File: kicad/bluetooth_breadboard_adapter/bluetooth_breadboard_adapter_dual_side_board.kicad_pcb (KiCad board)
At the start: 2 copper layers, 24.9 x 36.1 mm, 4 parts, among them J1 SCJ368R1NUS0B00G, P1 CONNECTOR, P2 CONNECTOR, U1 BLK-MD-SPK-B

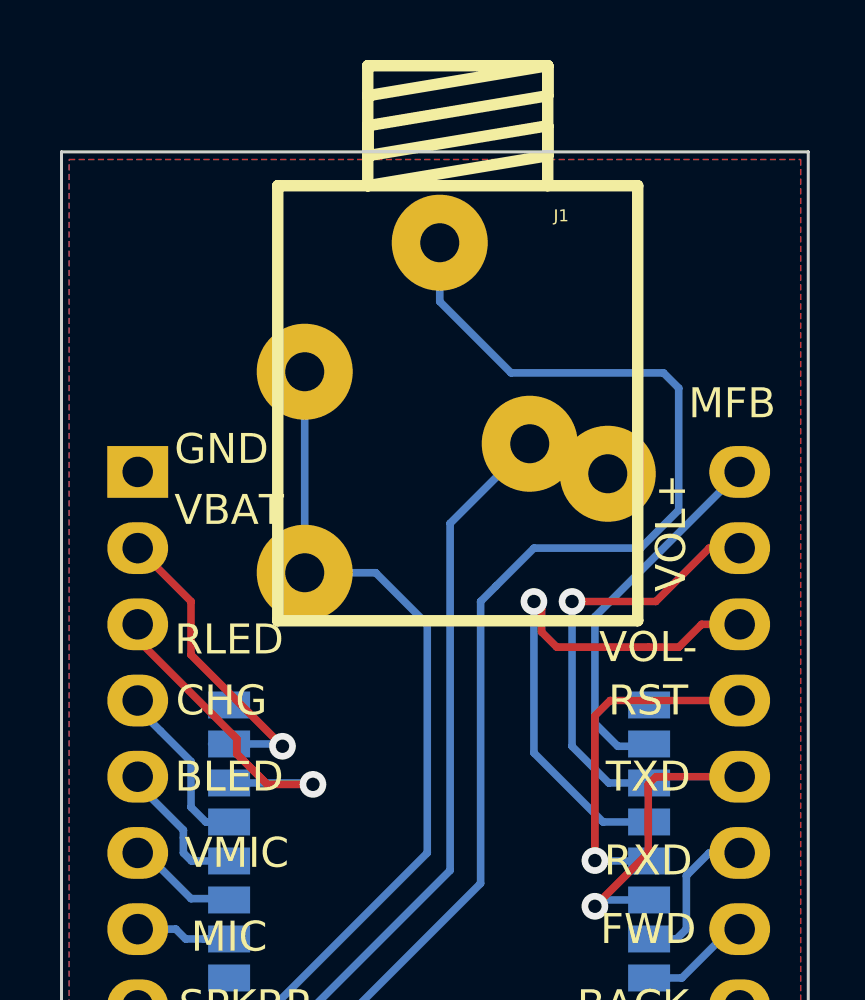
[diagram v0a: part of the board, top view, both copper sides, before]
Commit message: update patch to modules becouse of changed library name
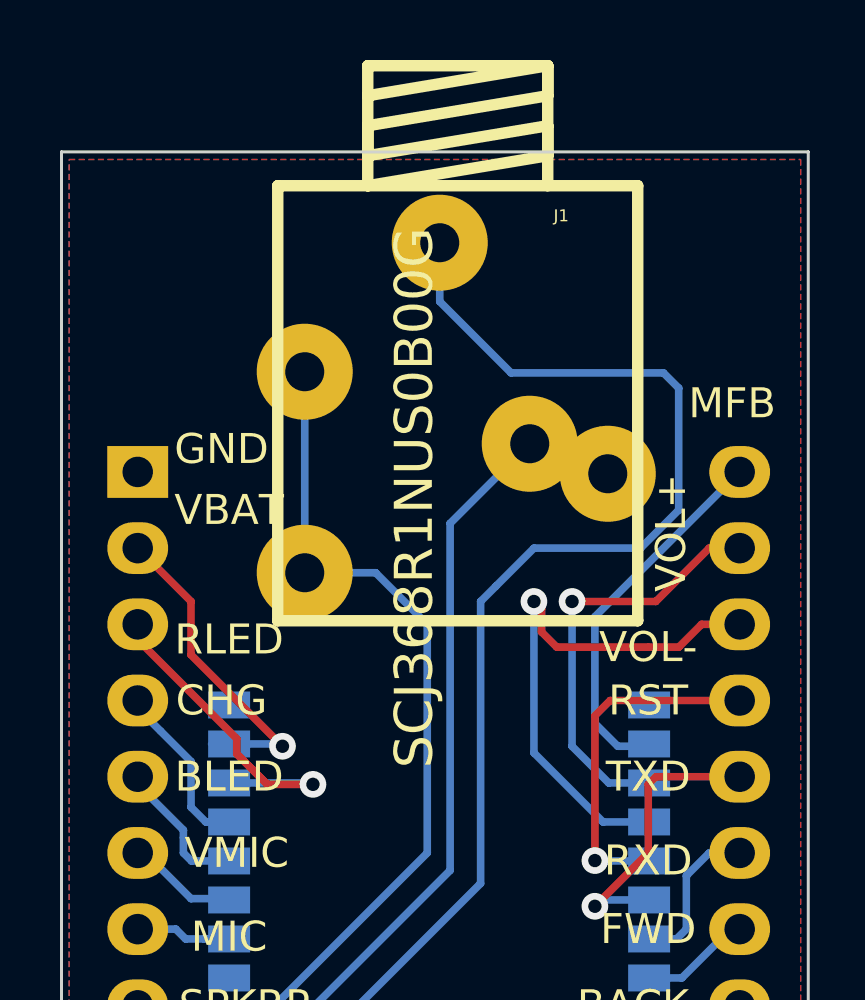
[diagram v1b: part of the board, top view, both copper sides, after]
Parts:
- J1: footprint 3.5mm stereo jack:3.5mm_stereo_jack -> my_modules:3.5mm_stereo_jack
- U1: footprint BLK-MD-SPK-B.mod:BLK-MD-SPK-B -> my_modules:BLK-MD-SPK-B

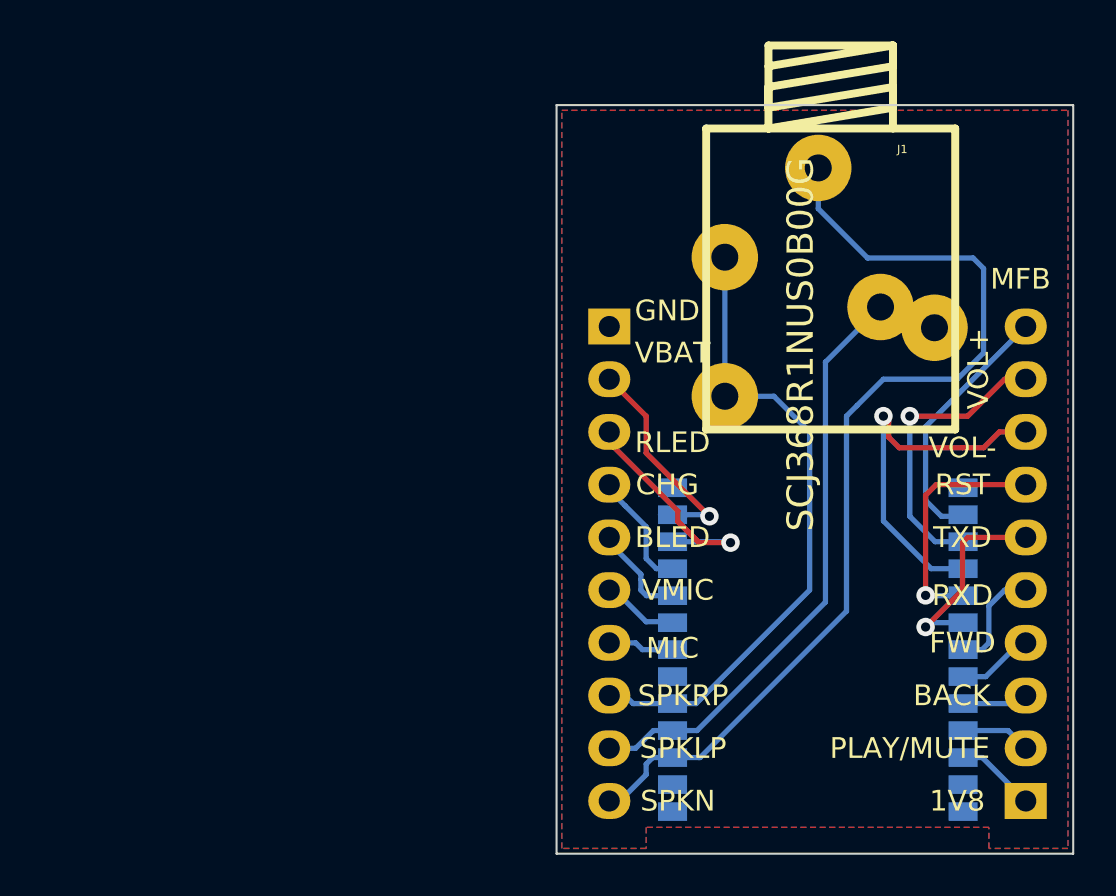
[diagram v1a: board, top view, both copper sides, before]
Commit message: bluetooth board update
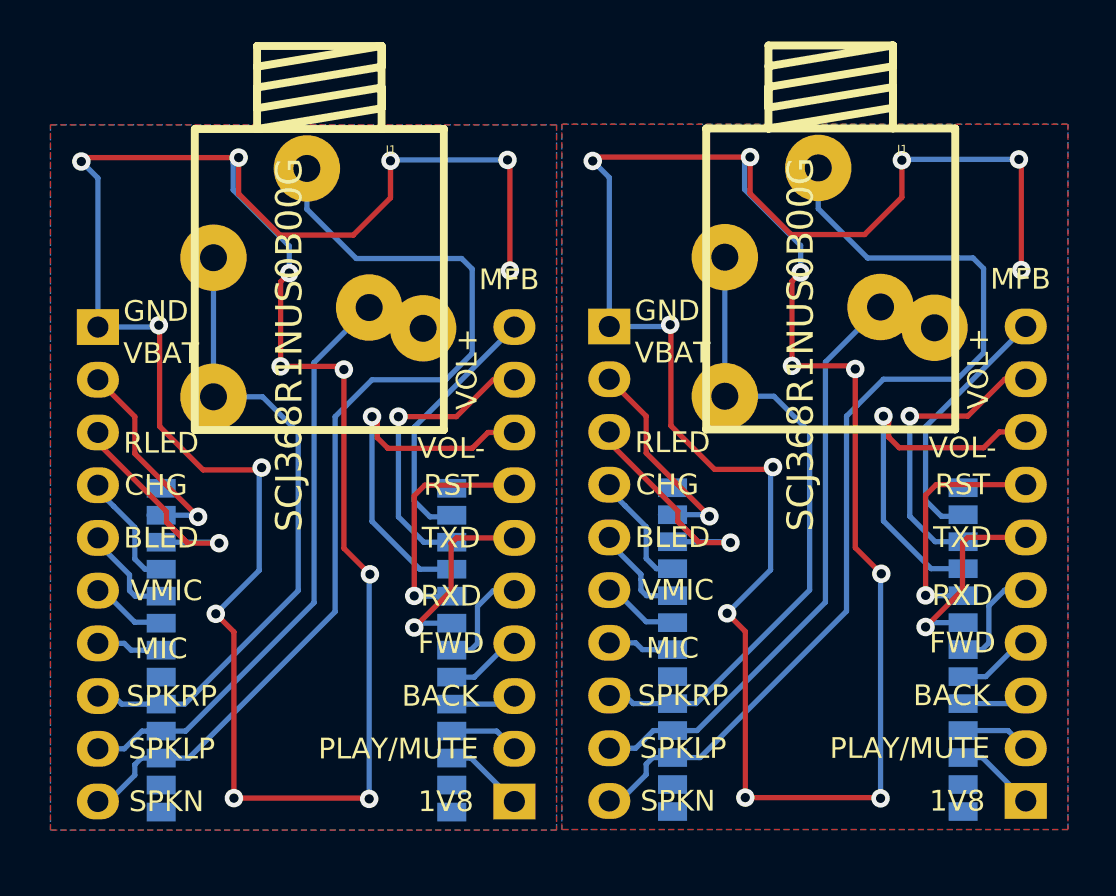
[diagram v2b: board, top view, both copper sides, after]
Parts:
- added J1: SCJ368R1NUS0B00G, my_modules:3.5mm_stereo_jack, F.Cu at (197.1, 137.4)
- added P1: CONNECTOR, Pin_Headers:Pin_Header_Straight_1x10, B.Cu at (206.5, 151.4)
- added P2: CONNECTOR, Pin_Headers:Pin_Header_Straight_1x10, B.Cu at (186.4, 151.4)
- added U1: BLK-MD-SPK-B, my_modules:BLK-MD-SPK-B, B.Cu at (188.2, 169.7)
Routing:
- net GND: track 0.00 -> 225.3 mm, vias 0 -> 28
- net Net-(J1-Pad1): track 48.3 -> 96.6 mm
- net Net-(J1-Pad4): track 33.6 -> 67.3 mm
- net Net-(J1-Pad2): track 32.6 -> 65.2 mm
- net Net-(P1-Pad8): track 18.1 -> 36.2 mm, vias 1 -> 2
- net Net-(P1-Pad9): track 15.8 -> 31.5 mm, vias 1 -> 2
- net Net-(P2-Pad3): track 13.0 -> 26.0 mm, vias 1 -> 2
- net Net-(P1-Pad10): track 12.5 -> 25.1 mm
- net Net-(P2-Pad2): track 11.8 -> 23.5 mm, vias 1 -> 2
- net Net-(P1-Pad7): track 11.7 -> 23.4 mm, vias 1 -> 2
- net Net-(P1-Pad6): track 9.85 -> 19.7 mm, vias 1 -> 2
- net Net-(P2-Pad4): track 5.89 -> 11.8 mm
- net Net-(P2-Pad5): track 5.44 -> 10.9 mm
- net Net-(P1-Pad5): track 5.25 -> 10.5 mm
- net Net-(P2-Pad7): track 4.27 -> 8.55 mm
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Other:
- board outline removed

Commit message: 3.5mm jack update to scj-0354-5PU
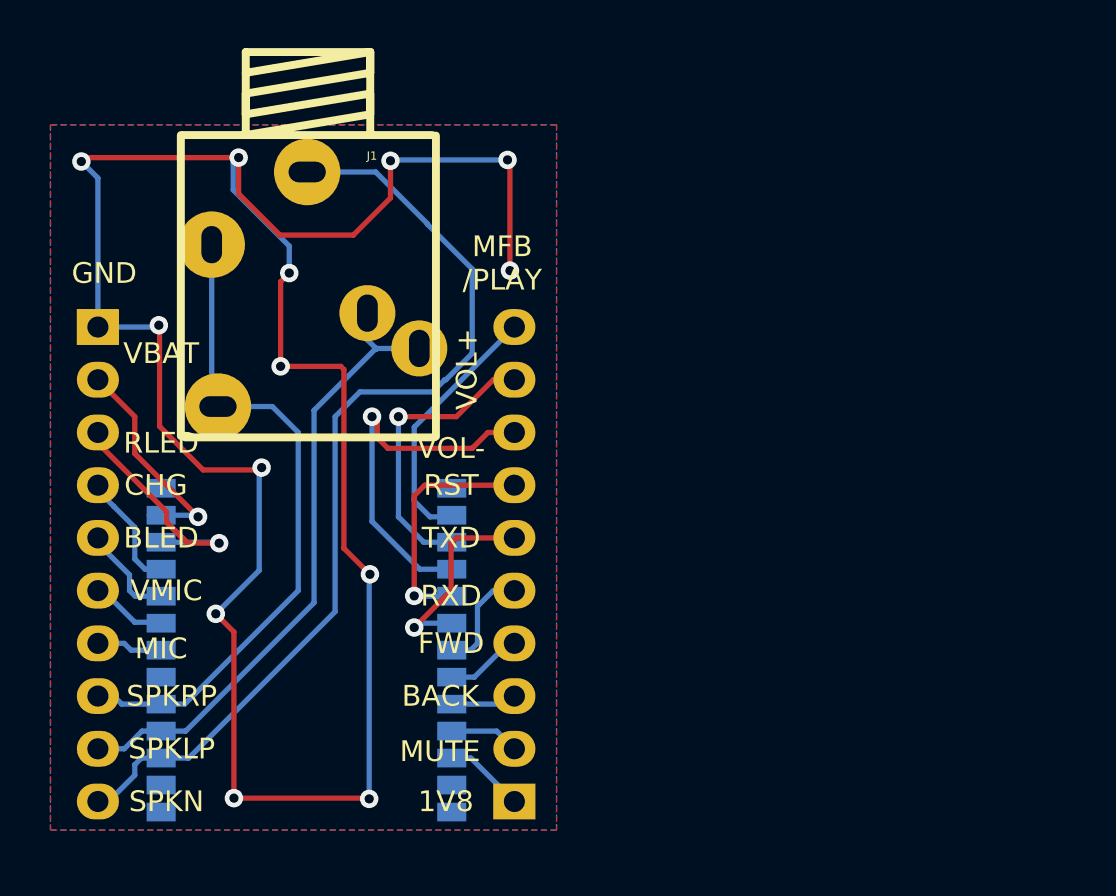
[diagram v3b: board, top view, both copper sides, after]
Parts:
- removed the J1 at (197.1, 137.4)
- removed the J1 at (221.7, 137.4)
- removed the P1 at (231.1, 151.4)
- removed the P2 at (211.1, 151.4)
- removed the U1 at (212.9, 169.7)
- added J1: SCJ-0354-5PU, jacks:SCJ-0354-5PU, F.Cu at (196.5, 130.8)
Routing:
- net GND: track 225.3 -> 112.7 mm, vias 28 -> 13
- net Net-(J1-Pad1): track 96.6 -> 48.1 mm
- net Net-(J1-Pad2): track 67.3 -> 32.7 mm
- net Net-(J1-Pad4): track 65.2 -> 33.4 mm
- net Net-(P1-Pad8): track 36.2 -> 18.1 mm, vias 2 -> 1
- net Net-(P1-Pad9): track 31.5 -> 15.8 mm, vias 2 -> 1
- net Net-(P2-Pad3): track 26.0 -> 13.0 mm, vias 2 -> 1
- net Net-(P1-Pad10): track 25.1 -> 12.5 mm
- net Net-(P2-Pad2): track 23.5 -> 11.8 mm, vias 2 -> 1
- net Net-(P1-Pad7): track 23.4 -> 11.7 mm, vias 2 -> 1
- net Net-(P1-Pad6): track 19.7 -> 9.85 mm, vias 2 -> 1
- net Net-(P2-Pad4): track 11.8 -> 5.89 mm
- net Net-(P2-Pad5): track 10.9 -> 5.44 mm
- net Net-(P1-Pad5): track 10.5 -> 5.25 mm
- net Net-(P2-Pad7): track 8.55 -> 4.27 mm
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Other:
- board text added: "MFB /PLAY"
- board text added: "MUTE"
- board text removed: "MFB"
- board text removed: "PLAY/MUTE"

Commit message: schematics with new kicad version
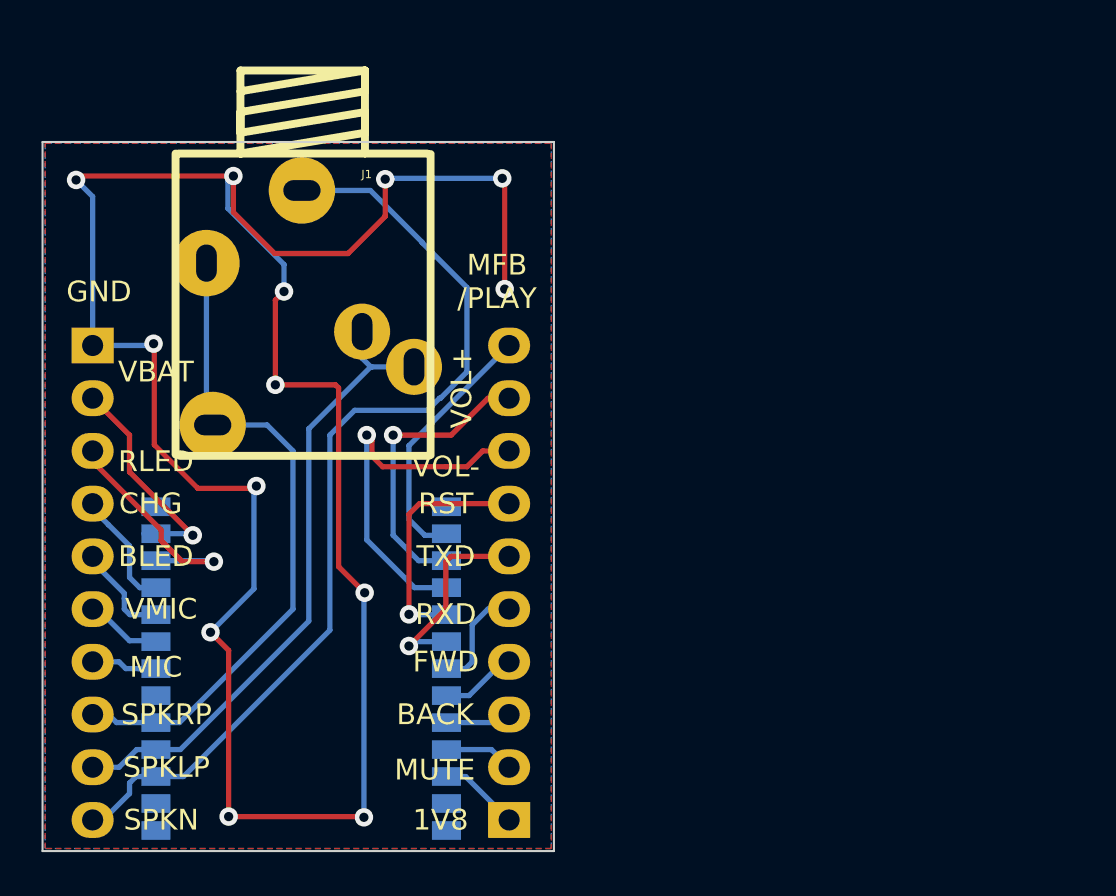
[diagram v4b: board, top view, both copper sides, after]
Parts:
- moved J1 0.92 mm to (196.3, 131.7)
- moved U1 0.92 mm to (188.0, 170.6)
- moved P1 0.92 mm to (206.2, 152.3)
- moved P2 0.92 mm to (186.2, 152.3)
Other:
- board outline added: 24.6 x 34.2 mm
